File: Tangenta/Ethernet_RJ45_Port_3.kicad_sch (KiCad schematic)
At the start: 2 parts, among them J7 HY911130A

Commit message: initialize branch
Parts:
- renumbered C1 to C165, J7 to J24
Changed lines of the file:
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@@
   (symbol (lib_id "power:GNDREF") (at 168.275 89.535 0) (mirror y) (unit 1)
     (in_bom yes) (on_board yes) (dnp no) (fields_autoplaced)
-    (property "Reference" "#PWR013" (at 168.275 95.885 0)
+    (property "Reference" "#PWR078" (at 168.275 95.885 0)
       (effects (font (size 1.27 1.27)) hide)
     )
@@
     (instances
       (project "Tangenta"
-        (path "/358d1bcf-7599-4352-8c4d-baa18a5f09e6/d6c05402-162e-441f-bed8-be7996260fb4"
-          (reference "#PWR013") (unit 1)
-        )
-        (path "/358d1bcf-7599-4352-8c4d-baa18a5f09e6/9b1f6f94-444c-4c59-8de9-290bde336856"
-          (reference "#PWR050") (unit 1)
-        )
-        (path "/358d1bcf-7599-4352-8c4d-baa18a5f09e6/9b1f6f94-444c-4c59-8de9-290bde336856/04648235-6c5e-4915-ab80-8fea22048f3c"
-          (reference "#PWR050") (unit 1)
-        )
-        (path "/358d1bcf-7599-4352-8c4d-baa18a5f09e6/2bb52479-7b35-496d-9807-27e706c6ef7b"
-          (reference "#PWR059") (unit 1)
-        )
-        (path "/358d1bcf-7599-4352-8c4d-baa18a5f09e6/2bb52479-7b35-496d-9807-27e706c6ef7b/c653b84e-94ee-4be9-b47c-8c767f88973e"
-          (reference "#PWR059") (unit 1)
-        )
-        (path "/358d1bcf-7599-4352-8c4d-baa18a5f09e6/2bb52479-7b35-496d-9807-27e706c6ef7b/107b1895-3302-473d-bd1c-b123cf003d25"
-          (reference "#PWR069") (unit 1)
-        )
         (path "/358d1bcf-7599-4352-8c4d-baa18a5f09e6/2bb52479-7b35-496d-9807-27e706c6ef7b/5dd23ea2-ad33-4f2c-a45e-3d59d95f0b2c"
           (reference "#PWR078") (unit 1)
@@
   (symbol (lib_id "power:GNDREF") (at 25.4 24.13 270) (mirror x) (unit 1)
     (in_bom yes) (on_board yes) (dnp no) (fields_autoplaced)
-    (property "Reference" "#PWR013" (at 19.05 24.13 0)
+    (property "Reference" "#PWR077" (at 19.05 24.13 0)
       (effects (font (size 1.27 1.27)) hide)
     )
@@
     (instances
       (project "Tangenta"
-        (path "/358d1bcf-7599-4352-8c4d-baa18a5f09e6/d6c05402-162e-441f-bed8-be7996260fb4"
-          (reference "#PWR013") (unit 1)
-        )
-        (path "/358d1bcf-7599-4352-8c4d-baa18a5f09e6/9b1f6f94-444c-4c59-8de9-290bde336856"
-          (reference "#PWR050") (unit 1)
-        )
-        (path "/358d1bcf-7599-4352-8c4d-baa18a5f09e6/9b1f6f94-444c-4c59-8de9-290bde336856/04648235-6c5e-4915-ab80-8fea22048f3c"
-          (reference "#PWR050") (unit 1)
-        )
-        (path "/358d1bcf-7599-4352-8c4d-baa18a5f09e6/2bb52479-7b35-496d-9807-27e706c6ef7b"
-          (reference "#PWR059") (unit 1)
-        )
-        (path "/358d1bcf-7599-4352-8c4d-baa18a5f09e6/2bb52479-7b35-496d-9807-27e706c6ef7b/c653b84e-94ee-4be9-b47c-8c767f88973e"
-          (reference "#PWR059") (unit 1)
-        )
         (path "/358d1bcf-7599-4352-8c4d-baa18a5f09e6/2bb52479-7b35-496d-9807-27e706c6ef7b/5dd23ea2-ad33-4f2c-a45e-3d59d95f0b2c"
           (reference "#PWR077") (unit 1)
@@
   (symbol (lib_id "CholaSymbolsPrjLib:C_Small") (at 124.46 70.485 270) (unit 1)
     (in_bom yes) (on_board yes) (dnp no)
-    (property "Reference" "C1" (at 120.65 69.215 90)
+    (property "Reference" "C165" (at 120.65 69.215 90)
       (effects (font (size 1.27 1.27)))
     )
@@
     (instances
       (project "Tangenta"
-        (path "/358d1bcf-7599-4352-8c4d-baa18a5f09e6/8215796b-9611-4f43-bcc5-319f8414b8a6"
-          (reference "C1") (unit 1)
-        )
-        (path "/358d1bcf-7599-4352-8c4d-baa18a5f09e6/d6c05402-162e-441f-bed8-be7996260fb4"
-          (reference "C9") (unit 1)
-        )
-        (path "/358d1bcf-7599-4352-8c4d-baa18a5f09e6/b1871a4d-6a35-44e2-a9a2-9a4af684371d"
-          (reference "C40") (unit 1)
-        )
-        (path "/358d1bcf-7599-4352-8c4d-baa18a5f09e6/6a8c68b5-4a7d-449e-86f6-34ced6d1cb55"
-          (reference "C81") (unit 1)
-        )
-        (path "/358d1bcf-7599-4352-8c4d-baa18a5f09e6/9b1f6f94-444c-4c59-8de9-290bde336856/04648235-6c5e-4915-ab80-8fea22048f3c"
-          (reference "C98") (unit 1)
-        )
-        (path "/358d1bcf-7599-4352-8c4d-baa18a5f09e6/2bb52479-7b35-496d-9807-27e706c6ef7b"
-          (reference "C157") (unit 1)
-        )
-        (path "/358d1bcf-7599-4352-8c4d-baa18a5f09e6/2bb52479-7b35-496d-9807-27e706c6ef7b/c653b84e-94ee-4be9-b47c-8c767f88973e"
-          (reference "C170") (unit 1)
-        )
-        (path "/358d1bcf-7599-4352-8c4d-baa18a5f09e6/2bb52479-7b35-496d-9807-27e706c6ef7b/8c8da075-62e5-4ec4-9abc-b27287749d5c"
-          (reference "C164") (unit 1)
-        )
-        (path "/358d1bcf-7599-4352-8c4d-baa18a5f09e6/2bb52479-7b35-496d-9807-27e706c6ef7b/107b1895-3302-473d-bd1c-b123cf003d25"
-          (reference "C173") (unit 1)
-        )
         (path "/358d1bcf-7599-4352-8c4d-baa18a5f09e6/2bb52479-7b35-496d-9807-27e706c6ef7b/5dd23ea2-ad33-4f2c-a45e-3d59d95f0b2c"
           (reference "C165") (unit 1)
@@
   (symbol (lib_id "CholaSymbolsPrjLib:HY911130A") (at 147.32 81.915 0) (unit 1)
     (in_bom yes) (on_board yes) (dnp no)
-    (property "Reference" "J7" (at 147.32 63.754 0)
+    (property "Reference" "J24" (at 147.32 63.754 0)
       (effects (font (size 1.27 1.27)))
     )
@@
     (instances
       (project "Tangenta"
-        (path "/358d1bcf-7599-4352-8c4d-baa18a5f09e6/2bb52479-7b35-496d-9807-27e706c6ef7b"
-          (reference "J7") (unit 1)
-        )
         (path "/358d1bcf-7599-4352-8c4d-baa18a5f09e6/2bb52479-7b35-496d-9807-27e706c6ef7b/5dd23ea2-ad33-4f2c-a45e-3d59d95f0b2c"
           (reference "J24") (unit 1)

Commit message: J6-J8,J22-J25,S1,U21
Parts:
- J24: footprint RJ45_MAGJACK:RJ45_MAGJACK_HY911130A -> CholaFootprintsPrjLib:RJ45_MAGJACK_HY911130A
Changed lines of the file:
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@@
       (effects (font (size 1.27 1.27)))
     )
-    (property "Footprint" "RJ45_MAGJACK:RJ45_MAGJACK_HY911130A" (at 168.91 104.775 0)
+    (property "Footprint" "CholaFootprintsPrjLib:RJ45_MAGJACK_HY911130A" (at 168.91 104.775 0)
       (effects (font (size 1.27 1.27) italic) hide)
     )

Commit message: Removing component association with previous project (local) libraries.
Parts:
- C165: symbol CholaSymbolsPrjLib:C_Small -> C_Small:C_Small
- J24: footprint CholaFootprintsPrjLib:RJ45_MAGJACK_HY911130A -> RJ45_MAGJACK_HY911130A:RJ45_MAGJACK_HY911130A; symbol CholaSymbolsPrjLib:HY911130A -> HY911130A:HY911130A
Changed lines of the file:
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@@
 	)
 	(symbol
-		(lib_id "CholaSymbolsPrjLib:C_Small")
+		(lib_id "C_Small:C_Small")
 		(at 124.46 70.485 270)
 		(unit 1)
@@
 	)
 	(symbol
-		(lib_id "CholaSymbolsPrjLib:HY911130A")
+		(lib_id "HY911130A:HY911130A")
 		(at 147.32 81.915 0)
 		(unit 1)
@@
 			)
 		)
-		(property "Footprint" "CholaFootprintsPrjLib:RJ45_MAGJACK_HY911130A"
+		(property "Footprint" "RJ45_MAGJACK_HY911130A:RJ45_MAGJACK_HY911130A"
 			(at 168.91 104.775 0)
 			(effects

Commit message: Fixes, continued...
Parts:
- C165: symbol C_Small:C_Small -> Device:C_Small
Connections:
- net GNDREF: no longer C165.2
- net at J24.1: no longer C165.1
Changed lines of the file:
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@@
 	)
 	(symbol
-		(lib_id "C_Small:C_Small")
+		(lib_id "Device:C_Small")
 		(at 124.46 70.485 270)
 		(unit 1)

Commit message: Fixes, continued...
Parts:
- C165: symbol Device:C_Small -> C_Small:C_Small
- J24: footprint RJ45_MAGJACK_HY911130A:RJ45_MAGJACK_HY911130A -> RJ45_MAGJACK:RJ45_MAGJACK_HY911130A
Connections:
- net GNDREF: now also C165.2
- net at J24.1: now also C165.1
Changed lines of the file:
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@@
 	)
 	(symbol
-		(lib_id "Device:C_Small")
+		(lib_id "C_Small:C_Small")
 		(at 124.46 70.485 270)
 		(unit 1)
@@
 			)
 		)
-		(property "Footprint" "RJ45_MAGJACK_HY911130A:RJ45_MAGJACK_HY911130A"
+		(property "Footprint" "RJ45_MAGJACK:RJ45_MAGJACK_HY911130A"
 			(at 168.91 104.775 0)
 			(effects

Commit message: Fixes, before checks.
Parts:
- C165: symbol C_Small:C_Small -> Device:C_Small
- J24: symbol HY911130A:HY911130A -> RJ45_MAGJACK:HY911130A
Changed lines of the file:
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@@
 	)
 	(symbol
-		(lib_id "C_Small:C_Small")
+		(lib_id "Device:C_Small")
 		(at 124.46 70.485 270)
 		(unit 1)
@@
 	)
 	(symbol
-		(lib_id "HY911130A:HY911130A")
+		(lib_id "RJ45_MAGJACK:HY911130A")
 		(at 147.32 81.915 0)
 		(unit 1)

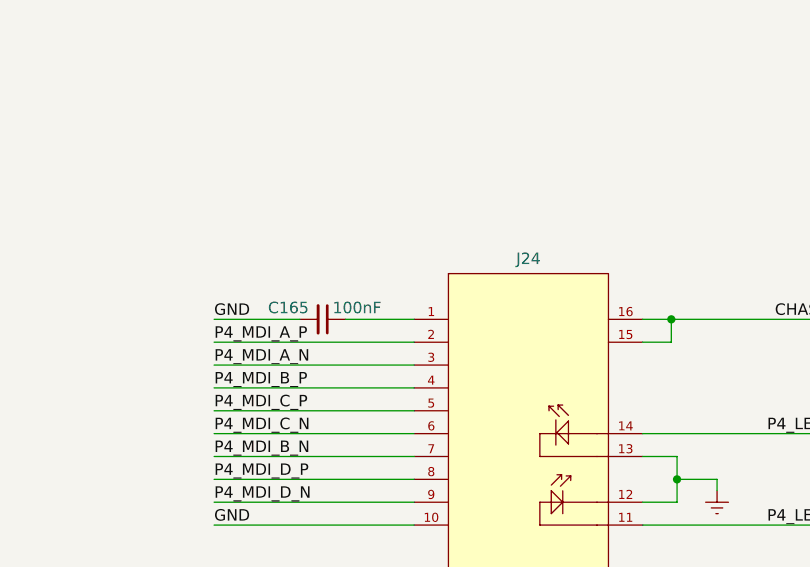
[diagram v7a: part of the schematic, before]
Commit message: Reverting to the original design.
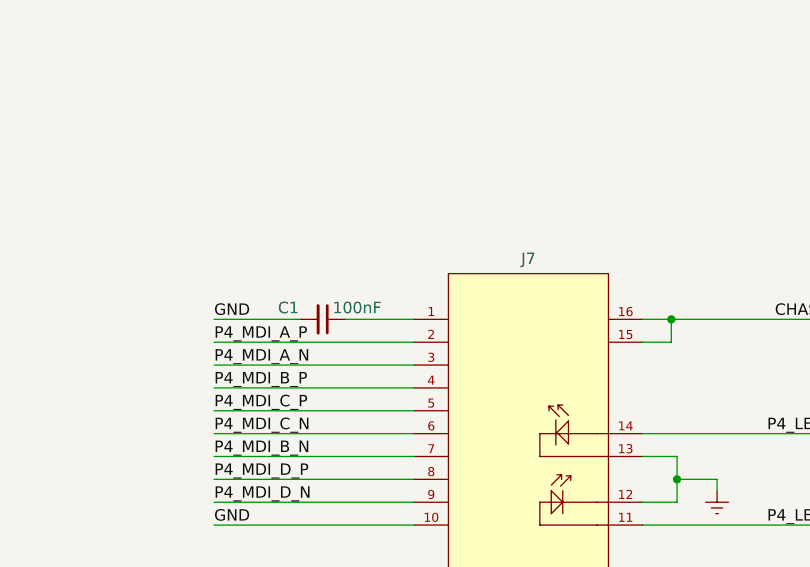
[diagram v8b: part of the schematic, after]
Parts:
- C1: renamed from C165; symbol Device:C_Small -> CholaSymbolsPrjLib:C_Small
- J7: renamed from J24; symbol RJ45_MAGJACK:HY911130A -> CholaSymbolsPrjLib:HY911130A
